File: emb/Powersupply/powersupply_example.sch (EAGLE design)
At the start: 13 parts, among them IC1 7805TV, IC2 7812TV, IC3 LM2574N-5.0

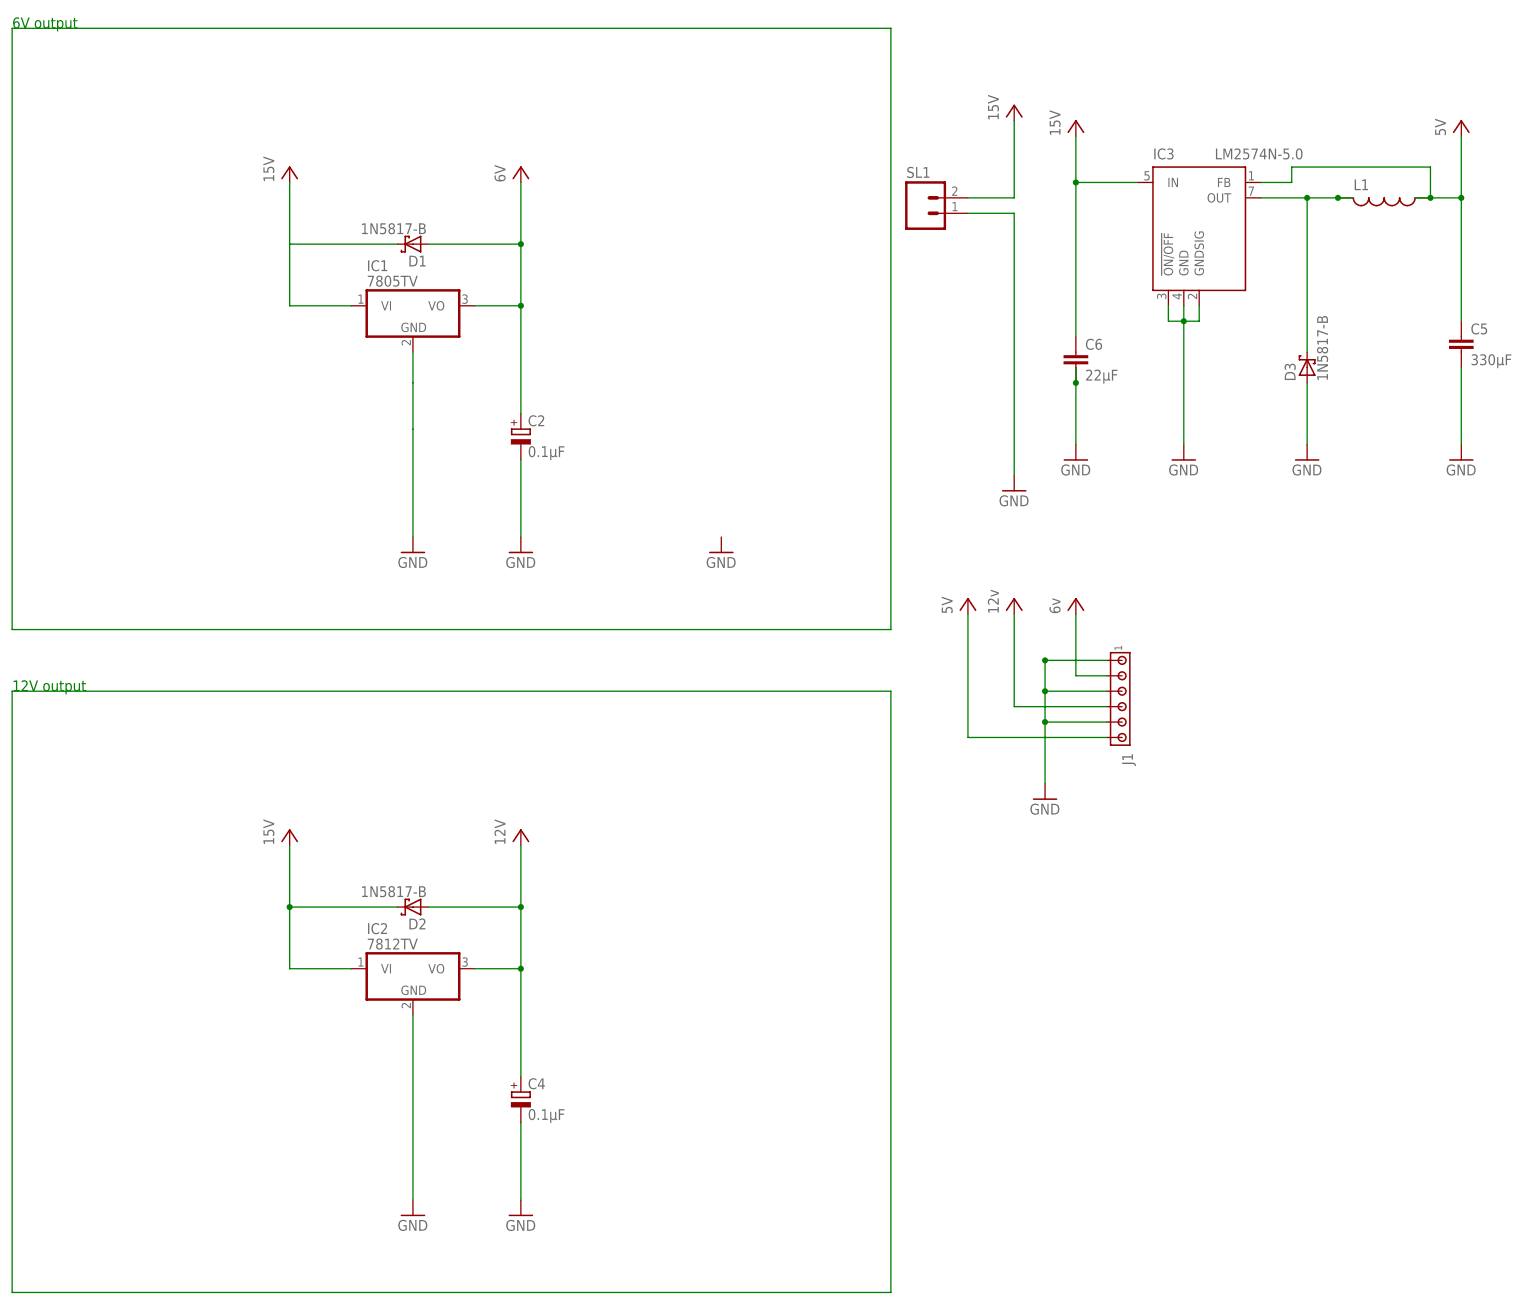
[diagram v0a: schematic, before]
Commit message: Communication both directions + updated power supply board
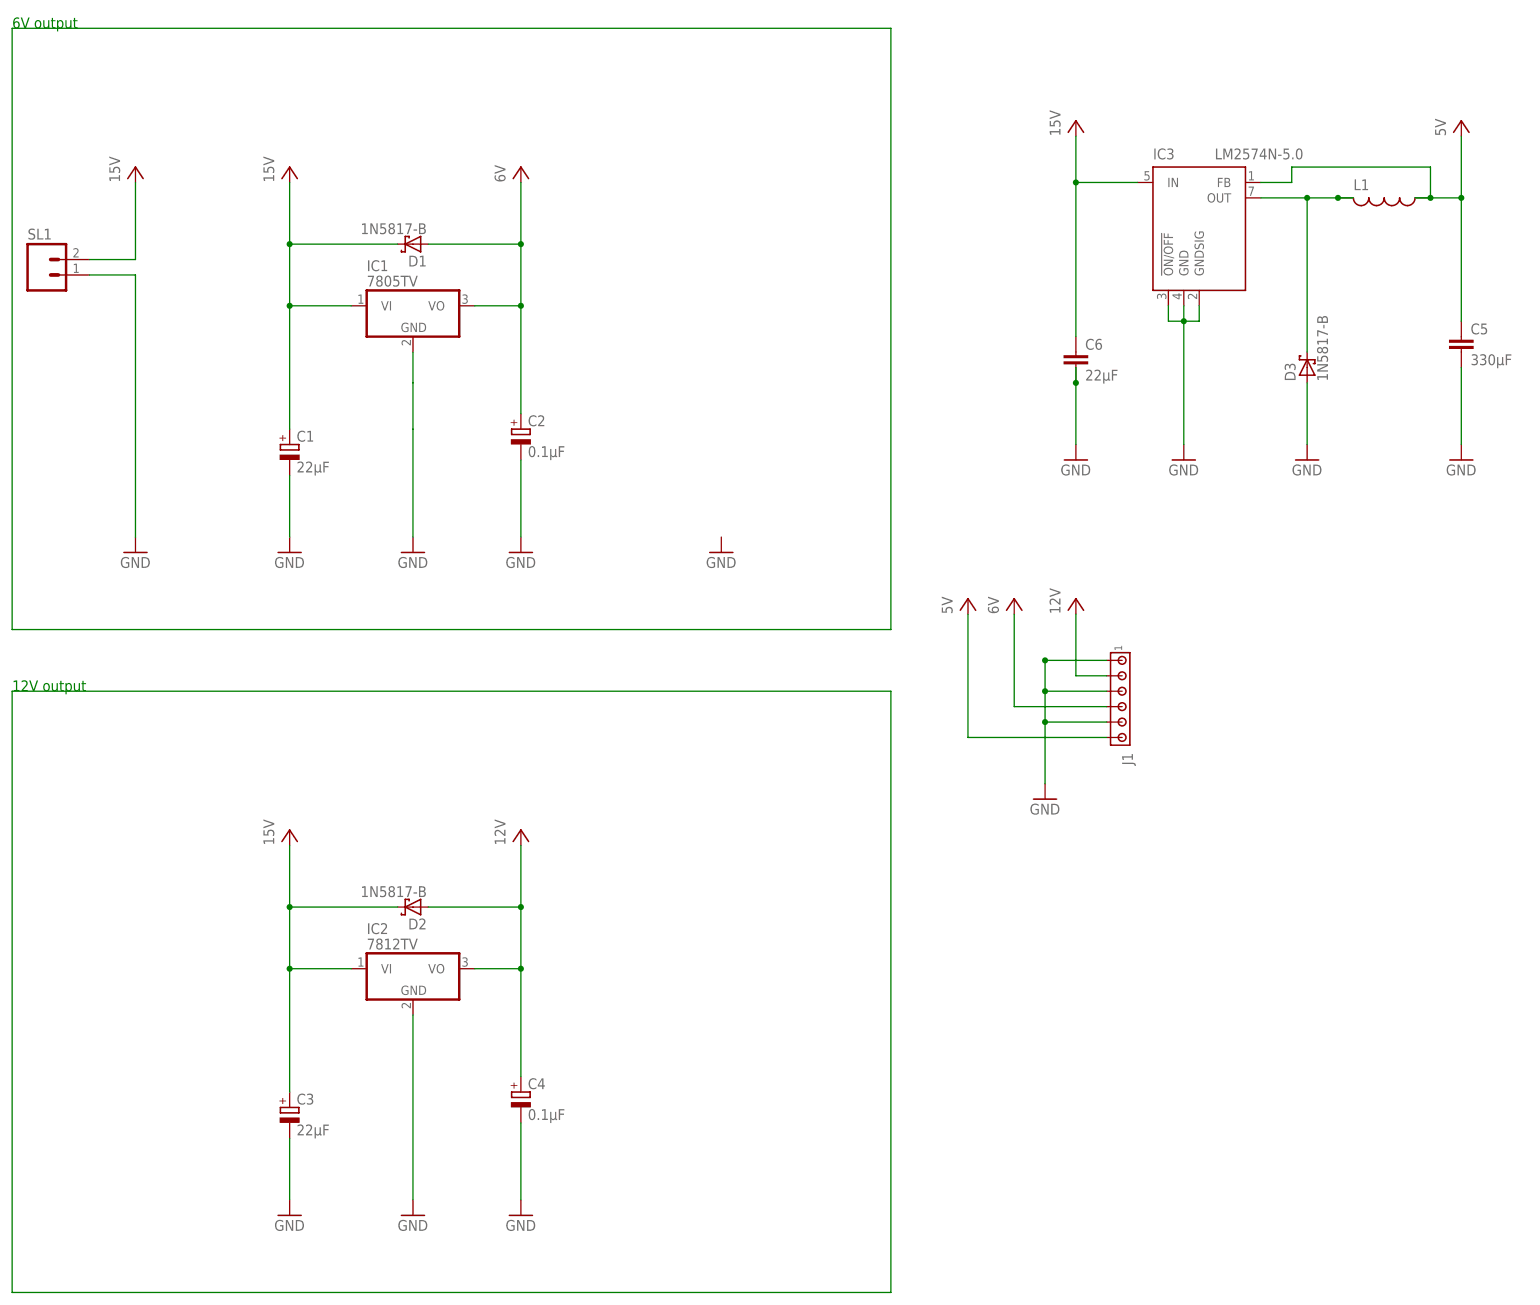
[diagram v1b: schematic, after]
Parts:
- added C1, C3: 22µF, rcl:CPOL-EUE2.5-5
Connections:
- net 12V: now also J1.2; no longer J1.4
- net 15V: now also C1.+, C3.+
- net 6V: now also J1.4; no longer J1.2
- net GND: now also C1.-, C3.-
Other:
- moved on the sheet: SL1
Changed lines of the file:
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@@
 <part name="P+2" library="supply1" deviceset="VCC" device="" value="15V"/>
 <part name="P+3" library="supply1" deviceset="VCC" device="" value="6V"/>
-<part name="P+4" library="supply1" deviceset="VCC" device="" value="12v"/>
+<part name="P+4" library="supply1" deviceset="VCC" device="" value="6V"/>
 <part name="SL1" library="con-amp-quick" deviceset="M02" device=""/>
 <part name="GND1" library="supply1" deviceset="GND" device=""/>
+<part name="GND2" library="supply1" deviceset="GND" device=""/>
 <part name="GND3" library="supply1" deviceset="GND" device=""/>
 <part name="GND4" library="supply1" deviceset="GND" device=""/>
 <part name="GND5" library="supply1" deviceset="GND" device=""/>
+<part name="C1" library="rcl" deviceset="CPOL-EU" device="E2.5-5" value="22µF"/>
 <part name="C2" library="rcl" deviceset="CPOL-EU" device="E2.5-5" value="0.1µF"/>
 <part name="D1" library="diode" deviceset="1N581*" device="" technology="7-B"/>
@@
 <part name="P+5" library="supply1" deviceset="VCC" device="" value="12V"/>
 <part name="P+6" library="supply1" deviceset="VCC" device="" value="5V"/>
+<part name="GND7" library="supply1" deviceset="GND" device=""/>
 <part name="GND8" library="supply1" deviceset="GND" device=""/>
 <part name="GND9" library="supply1" deviceset="GND" device=""/>
 <part name="GND10" library="supply1" deviceset="GND" device=""/>
+<part name="C3" library="rcl" deviceset="CPOL-EU" device="E2.5-5" value="22µF"/>
 <part name="C4" library="rcl" deviceset="CPOL-EU" device="E2.5-5" value="0.1µF"/>
 <part name="D2" library="diode" deviceset="1N581*" device="" technology="7-B"/>
@@
 <part name="GND12" library="supply1" deviceset="GND" device=""/>
 <part name="GND13" library="supply1" deviceset="GND" device=""/>
-<part name="P+8" library="supply1" deviceset="VCC" device="" value="6v"/>
+<part name="P+8" library="supply1" deviceset="VCC" device="" value="12V"/>
 <part name="5V" library="supply1" deviceset="VCC" device="" value="5V"/>
 <part name="L1" library="resistor" deviceset="L-US" device="0204/7"/>
@@
 </plain>
 <instances>
-<instance part="15V" gate="VCC" x="111.76" y="99.06"/>
+<instance part="15V" gate="VCC" x="-33.02" y="88.9"/>
 <instance part="P+2" gate="VCC" x="-7.62" y="88.9"/>
 <instance part="P+3" gate="VCC" x="30.48" y="88.9"/>
 <instance part="P+4" gate="VCC" x="111.76" y="17.78"/>
-<instance part="SL1" gate="G$1" x="96.52" y="81.28"/>
-<instance part="GND1" gate="1" x="111.76" y="35.56"/>
+<instance part="SL1" gate="G$1" x="-48.26" y="71.12"/>
+<instance part="GND1" gate="1" x="-33.02" y="25.4"/>
+<instance part="GND2" gate="1" x="-7.62" y="25.4"/>
 <instance part="GND3" gate="1" x="30.48" y="25.4"/>
 <instance part="GND4" gate="1" x="12.7" y="25.4"/>
 <instance part="GND5" gate="1" x="63.5" y="25.4"/>
+<instance part="C1" gate="G$1" x="-7.62" y="43.18"/>
 <instance part="C2" gate="G$1" x="30.48" y="45.72"/>
 <instance part="D1" gate="G$1" x="12.7" y="76.2" rot="R180"/>
@@
 <instance part="P+5" gate="VCC" x="30.48" y="-20.32"/>
 <instance part="P+6" gate="VCC" x="104.14" y="17.78"/>
+<instance part="GND7" gate="1" x="-7.62" y="-83.82"/>
 <instance part="GND8" gate="1" x="30.48" y="-83.82"/>
 <instance part="GND9" gate="1" x="12.7" y="-83.82"/>
 <instance part="GND10" gate="1" x="116.84" y="-15.24"/>
+<instance part="C3" gate="G$1" x="-7.62" y="-66.04"/>
 <instance part="C4" gate="G$1" x="30.48" y="-63.5"/>
 <instance part="D2" gate="G$1" x="12.7" y="-33.02" rot="R180"/>
@@
 <pinref part="GND1" gate="1" pin="GND"/>
 <pinref part="SL1" gate="G$1" pin="1"/>
-<wire x1="111.76" y1="38.1" x2="111.76" y2="81.28" width="0.1524" layer="91"/>
-<wire x1="111.76" y1="81.28" x2="104.14" y2="81.28" width="0.1524" layer="91"/>
+<wire x1="-33.02" y1="27.94" x2="-33.02" y2="71.12" width="0.1524" layer="91"/>
+<wire x1="-33.02" y1="71.12" x2="-40.64" y2="71.12" width="0.1524" layer="91"/>
 </segment>
 <segment>
@@
 </segment>
 <segment>
+<pinref part="C1" gate="G$1" pin="-"/>
+<pinref part="GND2" gate="1" pin="GND"/>
+<wire x1="-7.62" y1="38.1" x2="-7.62" y2="27.94" width="0.1524" layer="91"/>
+</segment>
+<segment>
 <pinref part="C2" gate="G$1" pin="-"/>
 <pinref part="GND3" gate="1" pin="GND"/>
@@
 <wire x1="12.7" y1="-81.28" x2="12.7" y2="-50.8" width="0.1524" layer="91"/>
 <pinref part="IC2" gate="A1" pin="GND"/>
+</segment>
+<segment>
+<pinref part="C3" gate="G$1" pin="-"/>
+<pinref part="GND7" gate="1" pin="GND"/>
+<wire x1="-7.62" y1="-71.12" x2="-7.62" y2="-81.28" width="0.1524" layer="91"/>
 </segment>
 <segment>
@@
 <pinref part="15V" gate="VCC" pin="VCC"/>
 <pinref part="SL1" gate="G$1" pin="2"/>
-<wire x1="111.76" y1="96.52" x2="111.76" y2="83.82" width="0.1524" layer="91"/>
-<wire x1="111.76" y1="83.82" x2="104.14" y2="83.82" width="0.1524" layer="91"/>
+<wire x1="-33.02" y1="86.36" x2="-33.02" y2="73.66" width="0.1524" layer="91"/>
+<wire x1="-33.02" y1="73.66" x2="-40.64" y2="73.66" width="0.1524" layer="91"/>
+</segment>
+<segment>
+<pinref part="P+2" gate="VCC" pin="VCC"/>
+<pinref part="C1" gate="G$1" pin="+"/>
+<wire x1="-7.62" y1="86.36" x2="-7.62" y2="76.2" width="0.1524" layer="91"/>
+<wire x1="-7.62" y1="76.2" x2="-7.62" y2="66.04" width="0.1524" layer="91"/>
+<wire x1="-7.62" y1="66.04" x2="-7.62" y2="45.72" width="0.1524" layer="91"/>
+<wire x1="10.16" y1="76.2" x2="-7.62" y2="76.2" width="0.1524" layer="91"/>
+<junction x="-7.62" y="76.2"/>
+<pinref part="D1" gate="G$1" pin="C"/>
+<pinref part="IC1" gate="A1" pin="VI"/>
+<wire x1="2.54" y1="66.04" x2="-7.62" y2="66.04" width="0.1524" layer="91"/>
+<junction x="-7.62" y="66.04"/>
 </segment>
 <segment>
 <pinref part="P+1" gate="VCC" pin="VCC"/>
+<pinref part="C3" gate="G$1" pin="+"/>
 <wire x1="-7.62" y1="-22.86" x2="-7.62" y2="-33.02" width="0.1524" layer="91"/>
 <wire x1="-7.62" y1="-33.02" x2="-7.62" y2="-43.18" width="0.1524" layer="91"/>
+<wire x1="-7.62" y1="-43.18" x2="-7.62" y2="-63.5" width="0.1524" layer="91"/>
 <wire x1="10.16" y1="-33.02" x2="-7.62" y2="-33.02" width="0.1524" layer="91"/>
 <junction x="-7.62" y="-33.02"/>
 <pinref part="D2" gate="G$1" pin="C"/>
 <wire x1="2.54" y1="-43.18" x2="-7.62" y2="-43.18" width="0.1524" layer="91"/>
+<junction x="-7.62" y="-43.18"/>
 <pinref part="IC2" gate="A1" pin="VI"/>
 </segment>
@@
 <wire x1="121.92" y1="60.96" x2="121.92" y2="86.36" width="0.1524" layer="91"/>
 <junction x="121.92" y="86.36"/>
-</segment>
-<segment>
-<pinref part="P+2" gate="VCC" pin="VCC"/>
-<wire x1="-7.62" y1="86.36" x2="-7.62" y2="76.2" width="0.1524" layer="91"/>
-<pinref part="D1" gate="G$1" pin="C"/>
-<wire x1="10.16" y1="76.2" x2="-7.62" y2="76.2" width="0.1524" layer="91"/>
-<pinref part="IC1" gate="A1" pin="VI"/>
-<wire x1="2.54" y1="66.04" x2="-7.62" y2="66.04" width="0.1524" layer="91"/>
-<wire x1="-7.62" y1="76.2" x2="-7.62" y2="66.04" width="0.1524" layer="91"/>
 </segment>
 </net>
@@
 </segment>
 <segment>
-<pinref part="P+8" gate="VCC" pin="VCC"/>
-<pinref part="J1" gate="G$1" pin="2"/>
-<wire x1="121.92" y1="15.24" x2="121.92" y2="5.08" width="0.1524" layer="91"/>
-<wire x1="121.92" y1="5.08" x2="127" y2="5.08" width="0.1524" layer="91"/>
+<pinref part="P+4" gate="VCC" pin="VCC"/>
+<pinref part="J1" gate="G$1" pin="4"/>
+<wire x1="111.76" y1="15.24" x2="111.76" y2="0" width="0.1524" layer="91"/>
+<wire x1="111.76" y1="0" x2="127" y2="0" width="0.1524" layer="91"/>
 </segment>
 </net>
@@
 </segment>
 <segment>
-<pinref part="P+4" gate="VCC" pin="VCC"/>
-<pinref part="J1" gate="G$1" pin="4"/>
-<wire x1="111.76" y1="15.24" x2="111.76" y2="0" width="0.1524" layer="91"/>
-<wire x1="111.76" y1="0" x2="127" y2="0" width="0.1524" layer="91"/>
-</segment>
-</net>
+<pinref part="P+8" gate="VCC" pin="VCC"/>
+<pinref part="J1" gate="G$1" pin="2"/>
+<wire x1="121.92" y1="15.24" x2="121.92" y2="5.08" width="0.1524" layer="91"/>
+<wire x1="121.92" y1="5.08" x2="127" y2="5.08" width="0.1524" layer="91"/>
+</segment>
+</net>
